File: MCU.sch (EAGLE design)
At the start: 2 parts, among them U1 ATXMEGA128A4U-AU

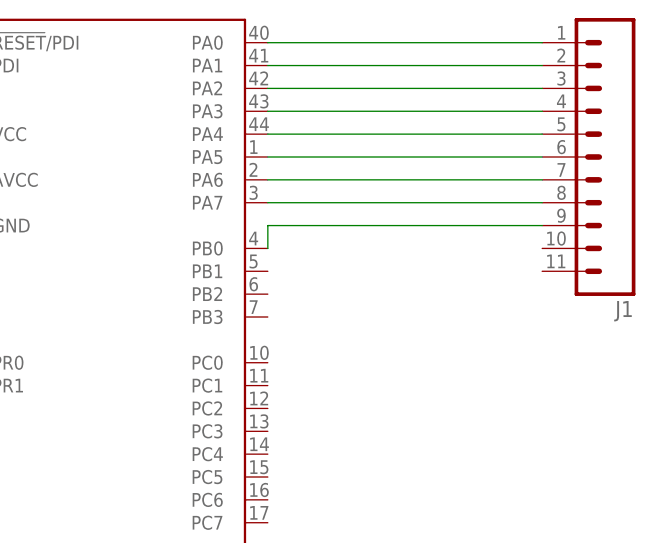
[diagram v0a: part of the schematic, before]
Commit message: Added a line to MCU board.
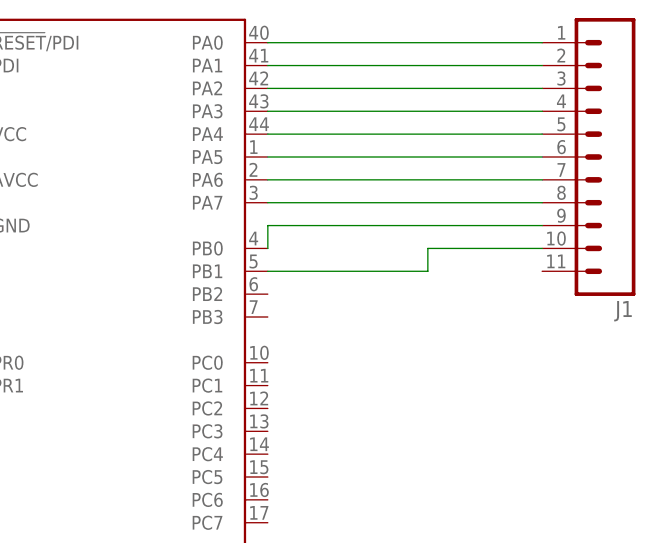
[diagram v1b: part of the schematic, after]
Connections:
- new net N$10: J1.10, U1.PB1
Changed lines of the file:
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@@
 <?xml version="1.0" encoding="utf-8"?>
 <!DOCTYPE eagle SYSTEM "eagle.dtd">
-<eagle version="8.1.1">
+<eagle version="7.5.0">
 <drawing>
 <settings>
@@
 </segment>
 </net>
+<net name="N$10" class="0">
+<segment>
+<pinref part="U1" gate="G$1" pin="PB1"/>
+<wire x1="88.9" y1="-27.94" x2="106.68" y2="-27.94" width="0.1524" layer="91"/>
+<wire x1="106.68" y1="-27.94" x2="106.68" y2="-25.4" width="0.1524" layer="91"/>
+<pinref part="J1" gate="G$1" pin="10"/>
+<wire x1="106.68" y1="-25.4" x2="119.38" y2="-25.4" width="0.1524" layer="91"/>
+</segment>
+</net>

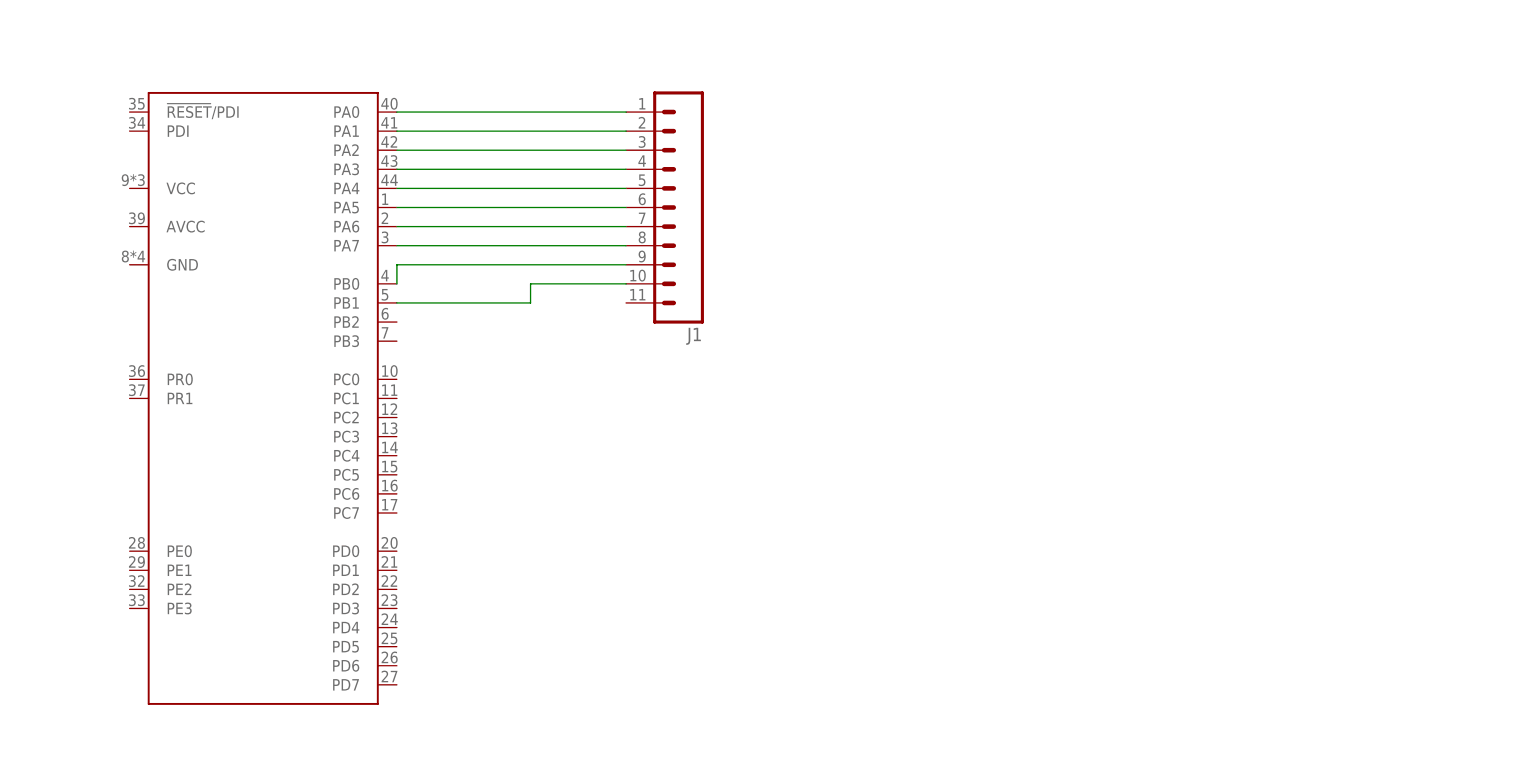
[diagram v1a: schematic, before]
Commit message: Redid schematic for MCU; cleaned up wires by replacing with busses.
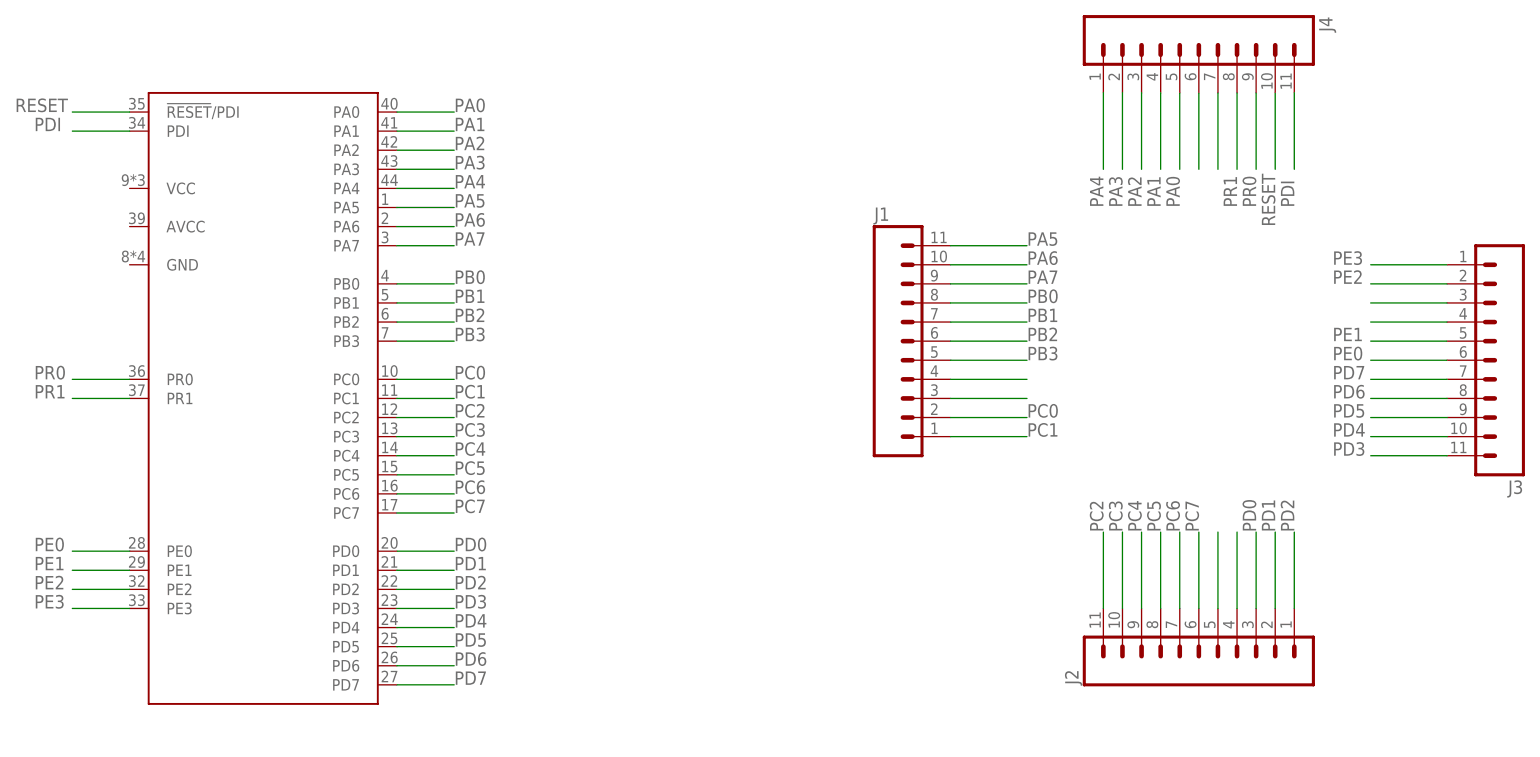
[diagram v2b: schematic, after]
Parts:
- added J2, J3, J4: (no value), SparkFun-Connectors:M11LONGPADS
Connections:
- removed net N$1: J1.1, U1.PA0
- removed net N$2: J1.2, U1.PA1
- removed net N$5: J1.5, U1.PA4
- removed net N$6: J1.6, U1.PA5
- new net N$12: J4.6
- new net N$13: J4.7
- new net PA0: J4.5, U1.PA0
- new net PA1: J4.4, U1.PA1
- new net PA2: J4.3, U1.PA2
- new net PA3: J4.2, U1.PA3
- new net PA4: J4.1, U1.PA4
- new net PA5: J1.11, U1.PA5
- new net PA6: J1.10, U1.PA6
- new net PA7: J1.9, U1.PA7
- new net PB0: J1.8, U1.PB0
- new net PB1: J1.7, U1.PB1
- new net PB2: J1.6, U1.PB2
- new net PB3: J1.5, U1.PB3
- new net PC0: J1.2, U1.PC0
- new net PC1: J1.1, U1.PC1
- new net PC2: J2.11, U1.PC2
- new net PC3: J2.10, U1.PC3
- new net PC4: J2.9, U1.PC4
- new net PC5: J2.8, U1.PC5
- new net PC6: J2.7, U1.PC6
- new net PC7: J2.6, U1.PC7
- new net PD0: J2.3, U1.PD0
- new net PD1: J2.2, U1.PD1
- new net PD2: J2.1, U1.PD2
- new net PD3: J3.11, U1.PD3
- new net PD4: J3.10, U1.PD4
- new net PD5: J3.9, U1.PD5
- new net PD6: J3.8, U1.PD6
- new net PD7: J3.7, U1.PD7
- new net PDI: J4.11, U1.PDI
- new net PE0: J3.6, U1.PE0
- new net PE1: J3.5, U1.PE1
- new net PE2: J3.2, U1.PE2
- new net PE3: J3.1, U1.PE3
- new net PR0: J4.9, U1.PR0
- new net PR1: J4.8, U1.PR1
- new net RESET: J4.10, U1.!RESET!/PDI
- net N$10: now also J2.4; no longer J1.10, U1.PB1
- net N$3: now also J3.3; no longer J1.3, U1.PA2
- net N$4: now also J3.4; no longer J1.4, U1.PA3
- net N$7: now also J2.5; no longer J1.7, U1.PA6
- net N$8: now also J1.4; no longer J1.8, U1.PA7
- net N$9: now also J1.3; no longer J1.9, U1.PB0
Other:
- moved on the sheet: J1

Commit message: Added decoupling capacitors to VCC.
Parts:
- added C1, C2, C3, C4, C5: (no value), resistor:C-USC0805
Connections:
- new net GND: U1.GND
- new net VCC: U1.VCC
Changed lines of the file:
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@@
 <part name="J3" library="SparkFun-Connectors" deviceset="M11" device="LONGPADS"/>
 <part name="J4" library="SparkFun-Connectors" deviceset="M11" device="LONGPADS"/>
+<part name="GND1" library="supply1" deviceset="GND" device=""/>
+<part name="VCC" library="supply1" deviceset="VCC" device="" value="3.3V"/>
+<part name="VCC1" library="supply1" deviceset="VCC" device="" value="3.3V"/>
+<part name="VCC2" library="supply1" deviceset="VCC" device="" value="3.3V"/>
+<part name="VCC3" library="supply1" deviceset="VCC" device="" value="3.3V"/>
+<part name="VCC4" library="supply1" deviceset="VCC" device="" value="3.3V"/>
+<part name="VCC5" library="supply1" deviceset="VCC" device="" value="3.3V"/>
+<part name="C1" library="resistor" deviceset="C-US" device="C0805"/>
+<part name="C2" library="resistor" deviceset="C-US" device="C0805"/>
+<part name="C3" library="resistor" deviceset="C-US" device="C0805"/>
+<part name="C4" library="resistor" deviceset="C-US" device="C0805"/>
+<part name="C5" library="resistor" deviceset="C-US" device="C0805"/>
 </parts>
 <sheets>
@@
 <instance part="J3" gate="G$1" x="238.76" y="-35.56" rot="R180"/>
 <instance part="J4" gate="G$1" x="195.58" y="10.16" rot="R270"/>
+<instance part="GND1" gate="1" x="48.26" y="-25.4"/>
+<instance part="VCC" gate="VCC" x="50.8" y="-10.16"/>
+<instance part="VCC1" gate="VCC" x="121.92" y="-71.12"/>
+<instance part="VCC2" gate="VCC" x="129.54" y="-71.12"/>
+<instance part="VCC3" gate="VCC" x="137.16" y="-71.12"/>
+<instance part="VCC4" gate="VCC" x="144.78" y="-71.12"/>
+<instance part="VCC5" gate="VCC" x="152.4" y="-71.12"/>
+<instance part="C1" gate="G$1" x="121.92" y="-81.28"/>
+<instance part="C2" gate="G$1" x="129.54" y="-81.28"/>
+<instance part="C3" gate="G$1" x="137.16" y="-81.28"/>
+<instance part="C4" gate="G$1" x="144.78" y="-81.28"/>
+<instance part="C5" gate="G$1" x="152.4" y="-81.28"/>
 </instances>
 <busses>
@@
 </segment>
 </net>
+<net name="GND" class="0">
+<segment>
+<pinref part="GND1" gate="1" pin="GND"/>
+<pinref part="U1" gate="G$1" pin="GND"/>
+<wire x1="48.26" y1="-22.86" x2="53.34" y2="-22.86" width="0.1524" layer="91"/>
+</segment>
+</net>
+<net name="VCC" class="0">
+<segment>
+<pinref part="U1" gate="G$1" pin="VCC"/>
+<pinref part="VCC" gate="VCC" pin="VCC"/>
+<wire x1="53.34" y1="-12.7" x2="50.8" y2="-12.7" width="0.1524" layer="91"/>
+</segment>
+</net>
